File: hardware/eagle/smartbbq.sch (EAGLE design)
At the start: 24 parts, among them X1 KLBR1, X2 KLBR1, X3 KLBR1, X4 KLBR1

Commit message: LCD & driver
LCD, driver, values added and various other updates.
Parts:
- added C5: 10uF, adafruit:C-USC0805K
- added LED2: (no value), microbuilder:DISP_SEGMENT_4DIGIT_BL-Q56C43
- added R10, R9: 10K, adafruit:R-US_R0805
- added R11: 1K, rcl:R-US_R0603
- added U2: (no value), microbuilder:HT16K33_SOP28
- C1, C2, C3, C4: value (none) -> 10uF
- R1, R2, R3, R4: value (none) -> 10K
- R5, R6, R7, R8: value (none) -> 1K
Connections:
- new net +5V: C5.1, R10.1, R9.1, U$1.RAW, U2.VDD
- new net A0: LED2.P$8, U2.ROW2/A0
- new net A1: LED2.P$15, LED2.P$7, U2.ROW1/A1
- new net N$1: LED2.P$1, U2.COM0/AD
- new net N$2: LED2.P$2, U2.COM1/KS0
- new net N$20: LED2.P$11, U2.ROW5/K3
- new net N$21: LED2.P$12, U2.ROW6/K4
- new net N$22: LED2.P$5, U2.COM4
- new net N$23: LED2.P$9, U2.ROW3/K1
- new net N$24: LED2.P$10, U2.ROW4/K2
- new net N$25: LED2.P$6, U2.ROW0/A2
- new net N$26: R11.2, U$1.!RST
- new net N$27: LED2.P$13, U2.ROW7/K5
- new net N$3: LED2.P$4, U2.COM3/KS2
- new net N$4: LED2.P$3, U2.COM2/KS1
- net GND: now also C5.2, U$1.GND@2, U$1.GND@21, U2.VSS
- net HT16K33_SCL: now also R9.2, U2.SCL
- net HT16K33_SDA: now also R10.2, U2.SDA
- net N$15: now also R1.1; no longer R1.2
- net VCC: now also R1.2, R11.1; no longer R1.1
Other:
- moved on the sheet: C1, C2, C3, C4, LED_USR, LED_USR1, LED_USR2, LED_USR3, R1, R2, R3, R4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

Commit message: Piezo addition
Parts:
- added R12: 1K, rcl:R-US_R0603
- added U$2: CMT_1603_SMT, engirati:CMT_1603_SMT
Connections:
- new net N$28: R12.1, U$2.P$1
- new net N$29: U$1.A7, U$2.P$2
- net GND: now also R12.2
- net N$15: no longer U$1.A7
- net N$17: now also U$1.A5; no longer U$1.A6
- net N$18: now also U$1.A4; no longer U$1.A5
- net N$19: now also U$1.A3; no longer U$1.A4
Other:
- moved on the sheet: C1, C2, C3, C4, R1, R2, R3, R4, X1, X2, X3, X4

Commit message: Fans, power, misc
Added fan output and power circuitry.  Cleaned up a few random things.
Swapped 0603 parts for 0805.
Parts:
- removed U$1: SPARK_CORECORE, Spark:SPARK_CORECORE
- removed U$2: CMT_1603_SMT, engirati:CMT_1603_SMT
- removed X1, X2, X3, X4: KLBR1, con-lumberg:KLBR1
- added C6, C7: 10uF, rcl:C-USC0805
- added D1, D2, D3: FAIRCHILD_S1A_SMT, engirati:FAIRCHILD_S1A_SMT
- added J1, J2, J3, J4: MJ_2523_SMT, engirati:MJ_2523_SMT
- added J5: 5.5od/2.1id, engirati:PJ_002AH_SMT
- added J6, J7: 5.5od/2.5id, engirati:PJ_002AH_SMT
- added J8, J9: 22-05-7028-02, con-molex:22-05-7028-02
- added OK1: LTV826S, optocoupler:LTV826S
- added P1: CMT_1603_SMT, engirati:CMT_1603_SMT
- added Q1, Q2: NZT651, Fairchild_By_element14_Batch_1:NZT651
- added R13, R16: 10K, rcl:R-US_R0805
- added R14, R15, R17, R18: 330, rcl:R-US_R0805
- added SPARK: SPARK_CORECORE, Spark:SPARK_CORECORE
- added U1: (no value), microbuilder:HT16K33_SOP28
- C1, C2, C3, C4: device rcl:C-USC0603 -> rcl:C-USC0805
- C5: device adafruit:C-USC0805K -> rcl:C-USC0805
- R1, R12, R2, R3, R4: device rcl:R-US_R0603 -> rcl:R-US_R0805
- R10, R9: device adafruit:R-US_R0805 -> rcl:R-US_R0805
- R11: value 1K -> 10K; device rcl:R-US_R0603 -> rcl:R-US_R0805
- R5, R6, R7, R8: value 1K -> 330; device rcl:R-US_R0603 -> rcl:R-US_R0805
- U2: value (none) -> TLV1117-50IDCY; device microbuilder:HT16K33_SOP28 -> Texas Instruments_By_element14_Batch_1:TLV1117-33IDCY
- renumbered LED2 to LED1
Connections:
- new net +12V: C6.1, D1.C, D2.C, D3.C, J5.P$1, J6.P$1, J7.P$1, J8-1.S, J9-1.S, OK1A.COL, OK1B.A, U2.INPUT
- new net +3V3: R11.1, SPARK.VCC
- new net N$30: D2.A, J6.P$2, J6.P$3, J8-2.S, Q1.C, Q1.C_2
- new net N$31: Q2.B, R16.1
- new net N$32: OK1A.A, R14.1, R15.1
- new net N$33: OK1B.C, R16.2
- new net N$34: OK1A.EMIT, R13.2
- new net N$35: Q1.B, R13.1
- new net N$37: D3.A, J7.P$2, J7.P$3, J9-2.S, Q2.C, Q2.C_2
- new net N$38: OK1B.COL, R17.1, R18.1
- net +5V: now also C7.1, D1.A, SPARK.RAW, U1.VDD, U2.OUTPUT, U2.OUTPUT_2; no longer U$1.RAW, U2.VDD
- net A0: now also U1.ROW2/A0; no longer U2.ROW2/A0
- net A1: now also U1.ROW1/A1; no longer U2.ROW1/A1
- net FAN1: now also R14.2, R15.2, SPARK.A1; no longer U$1.A1
- net FAN2: now also R17.2, R18.2, SPARK.A0; no longer U$1.A0
- net GND: now also C6.2, C7.2, J1.P$2, J1.P$3, J2.P$2, J2.P$3, J3.P$2, J3.P$3, J4.P$2, J4.P$3, J5.P$2, J5.P$3, OK1A.C, OK1B.EMIT, Q1.E, Q2.E, SPARK.GND@2, SPARK.GND@21, U1.VSS, U2.ADJ/GND; no longer U$1.GND@2, U$1.GND@21, U2.VSS, X1.5, X2.5, X3.5, X4.5
- net HT16K33_SCL: now also SPARK.D1, U1.SCL; no longer U$1.D1, U2.SCL
- net HT16K33_SDA: now also SPARK.D0, U1.SDA; no longer U$1.D0, U2.SDA
- net N$1: now also U1.COM0/AD; no longer U2.COM0/AD
- net N$13: now also SPARK.D2; no longer U$1.D2
- net N$14: now also SPARK.D3; no longer U$1.D3
- net N$15: now also J1.P$1, SPARK.A6; no longer X1.3, X1.4
- net N$16: now also SPARK.A2; no longer U$1.A2
- net N$17: now also J2.P$1, SPARK.A5; no longer U$1.A5, X2.3, X2.4
- net N$18: now also J3.P$1, SPARK.A4; no longer U$1.A4, X3.3, X3.4
- net N$19: now also J4.P$1, SPARK.A3; no longer U$1.A3, X4.3, X4.4
- net N$2: now also U1.COM1/KS0; no longer U2.COM1/KS0
- net N$20: now also U1.ROW5/K3; no longer U2.ROW5/K3
- net N$21: now also U1.ROW6/K4; no longer U2.ROW6/K4
- net N$22: now also U1.COM4; no longer U2.COM4
- net N$23: now also U1.ROW3/K1; no longer U2.ROW3/K1
- net N$24: now also U1.ROW4/K2; no longer U2.ROW4/K2
- net N$25: now also U1.ROW0/A2; no longer U2.ROW0/A2
- net N$26: now also SPARK.!RST; no longer U$1.!RST
- net N$27: now also U1.ROW7/K5; no longer U2.ROW7/K5
- net N$28: now also P1.P$1; no longer U$2.P$1
- net N$29: now also P1.P$2, SPARK.A7; no longer U$1.A7, U$2.P$2
- net N$3: now also U1.COM3/KS2; no longer U2.COM3/KS2
- net N$4: now also U1.COM2/KS1; no longer U2.COM2/KS1
- net N$5: now also SPARK.D4; no longer U$1.D4
- net N$6: now also SPARK.D5; no longer U$1.D5
- net N$7: now also SPARK.D6; no longer U$1.D6
- net N$8: now also SPARK.D7; no longer U$1.D7
- net VCC: now also SPARK.VDDA; no longer R11.1, U$1.VCC, U$1.VDDA
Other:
- moved on the sheet: C1, C2, C3, C4, LED_USR, LED_USR1, LED_USR2, LED_USR3, R1, R11, R12, R2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

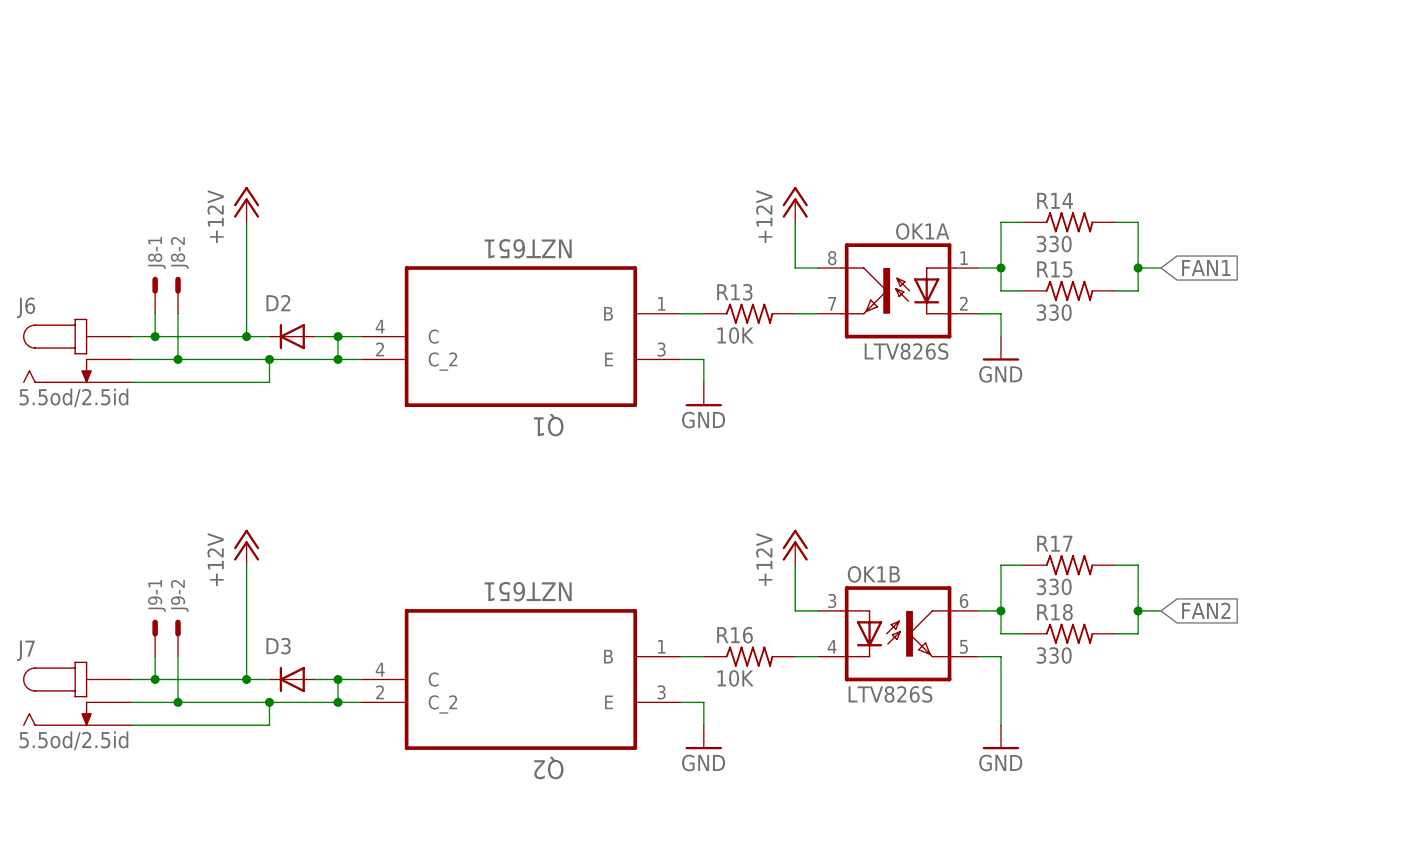
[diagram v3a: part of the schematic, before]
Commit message: Change fan driver circuitry
Updated fan driver circuitry to use single MOSFET.
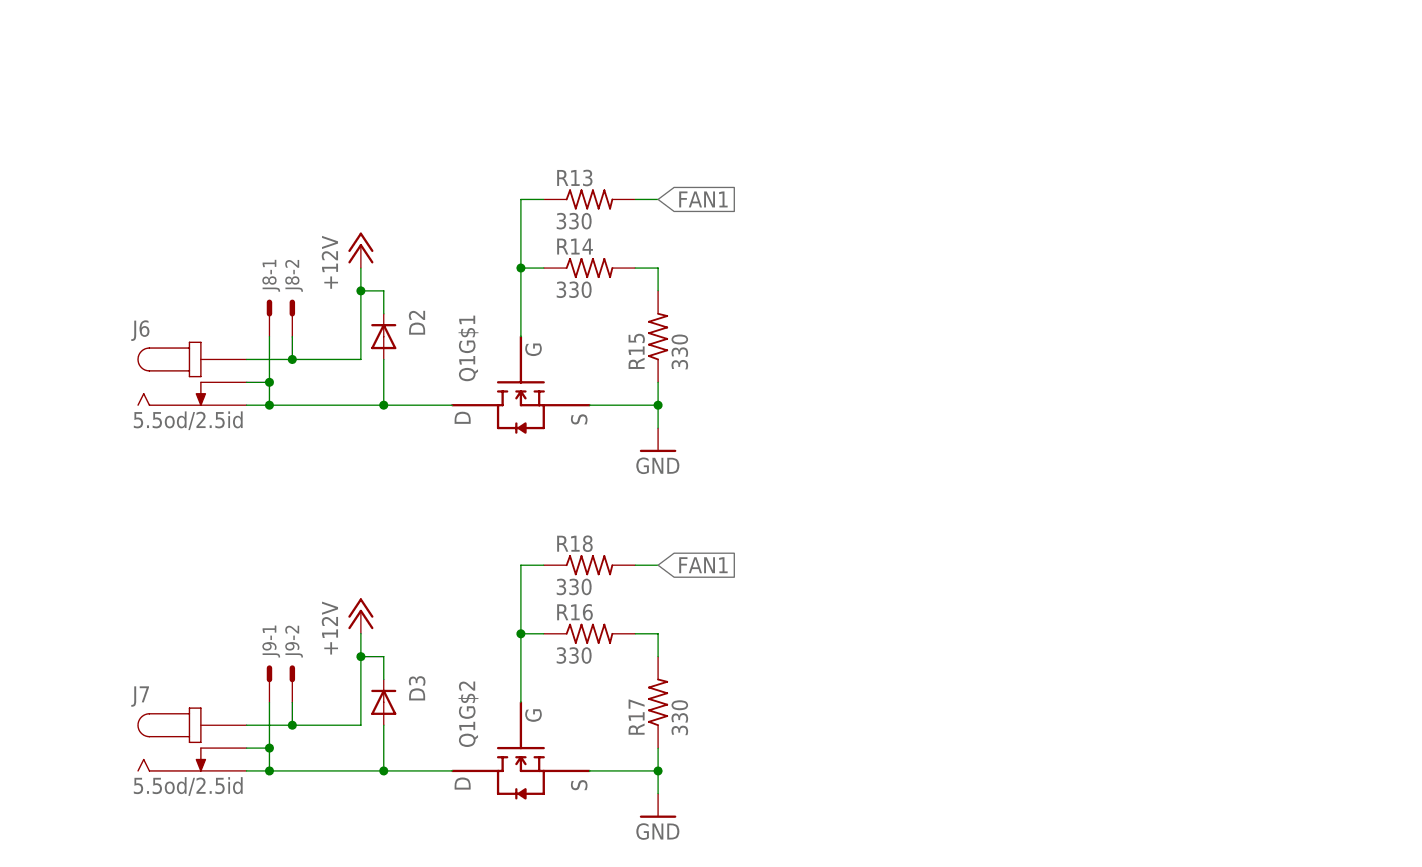
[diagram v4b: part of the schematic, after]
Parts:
- removed OK1: LTV826S, optocoupler:LTV826S
- removed Q2: NZT651, Fairchild_By_element14_Batch_1:NZT651
- Q1: value NZT651 -> SSM6N58NU; device Fairchild_By_element14_Batch_1:NZT651 -> engirati:SSM6N58NU
- R13, R16: value 10K -> 330
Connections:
- removed net N$37: D3.A, J7.P$2, J7.P$3, J9-2.S, Q2.C, Q2.C_2
- removed net N$38: OK1B.COL, R17.1, R18.1
- net +12V: now also J8-2.S, J9-2.S; no longer J8-1.S, J9-1.S, OK1A.COL, OK1B.A
- net FAN1: now also R13.2, R18.2; no longer R14.2, R15.2
- net FAN2: no longer R17.2, R18.2
- net GND: now also Q1G$1.P$1, Q1G$2.P$1, R15.1, R17.1; no longer OK1A.C, OK1B.EMIT, Q1.E, Q2.E
- net N$30: now also D3.A, J7.P$2, J7.P$3, J9-1.S, Q1G$2.P$3; no longer D2.A, J6.P$2, J6.P$3, J8-2.S, Q1.C, Q1.C_2
- net N$31: now also Q1G$2.P$2, R18.1; no longer Q2.B
- net N$32: now also D2.A, J6.P$2, J6.P$3, J8-1.S, Q1G$1.P$3; no longer OK1A.A, R14.1, R15.1
- net N$33: now also R17.2; no longer OK1B.C
- net N$34: now also Q1G$1.P$2, R13.1, R14.1; no longer OK1A.EMIT, R13.2
- net N$35: now also R14.2, R15.2; no longer Q1.B, R13.1
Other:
- moved on the sheet: D2, D3, J6, J7, J8-1, J8-2, J9-1, J9-2, R13, R14, R15, R16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
